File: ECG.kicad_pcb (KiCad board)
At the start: 4 copper layers, 60 x 60 mm, 94 parts, among them J1 SJ-3566AN, J2 Conn_01x02_Male, J3 Conn_01x08_Male, J4 Conn_01x02_Male, J5 Conn_ARM_JTAG_SWD_10, Q1 BC858, U1 ADR4525, U2 LTC3531, U3 INA333, U4 OPA388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

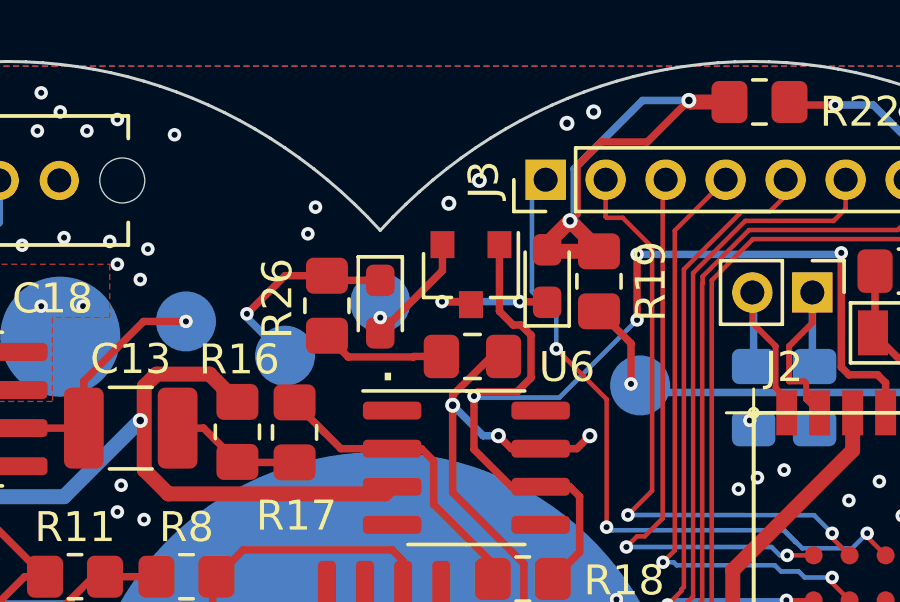
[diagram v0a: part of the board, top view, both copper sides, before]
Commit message: #24 - Update layout with flipped PNP and update images
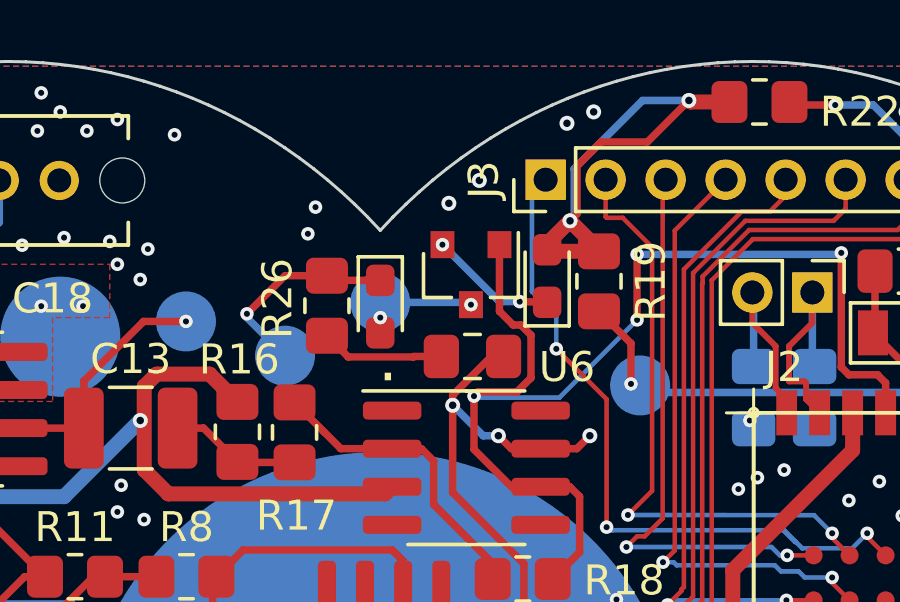
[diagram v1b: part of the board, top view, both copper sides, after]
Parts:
- R14: value 1k -> 10k
- R15: value 100k -> 10k
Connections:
- Q1 pad 2: Net-(D3-Pad2) -> Net-(D1-Pad1)
- Q1 pad 3: Net-(D1-Pad1) -> Net-(D3-Pad2)
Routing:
- net Net-(D3-Pad2): track 3.80 -> 3.20 mm, vias 1 -> 2

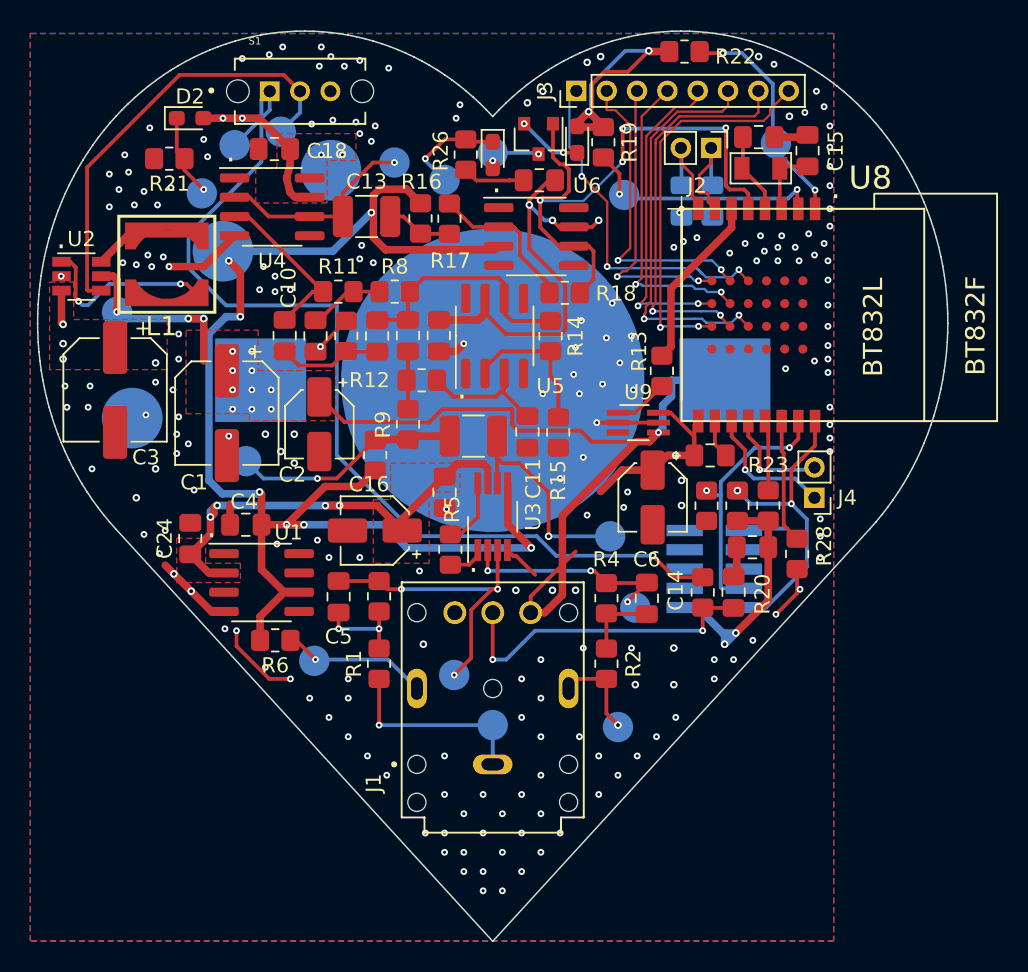
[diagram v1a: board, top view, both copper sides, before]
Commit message: Added mounting holes, Added lead-detect to a micro GPIO, and removed requirement that the leads must be attached prior to turning on the device
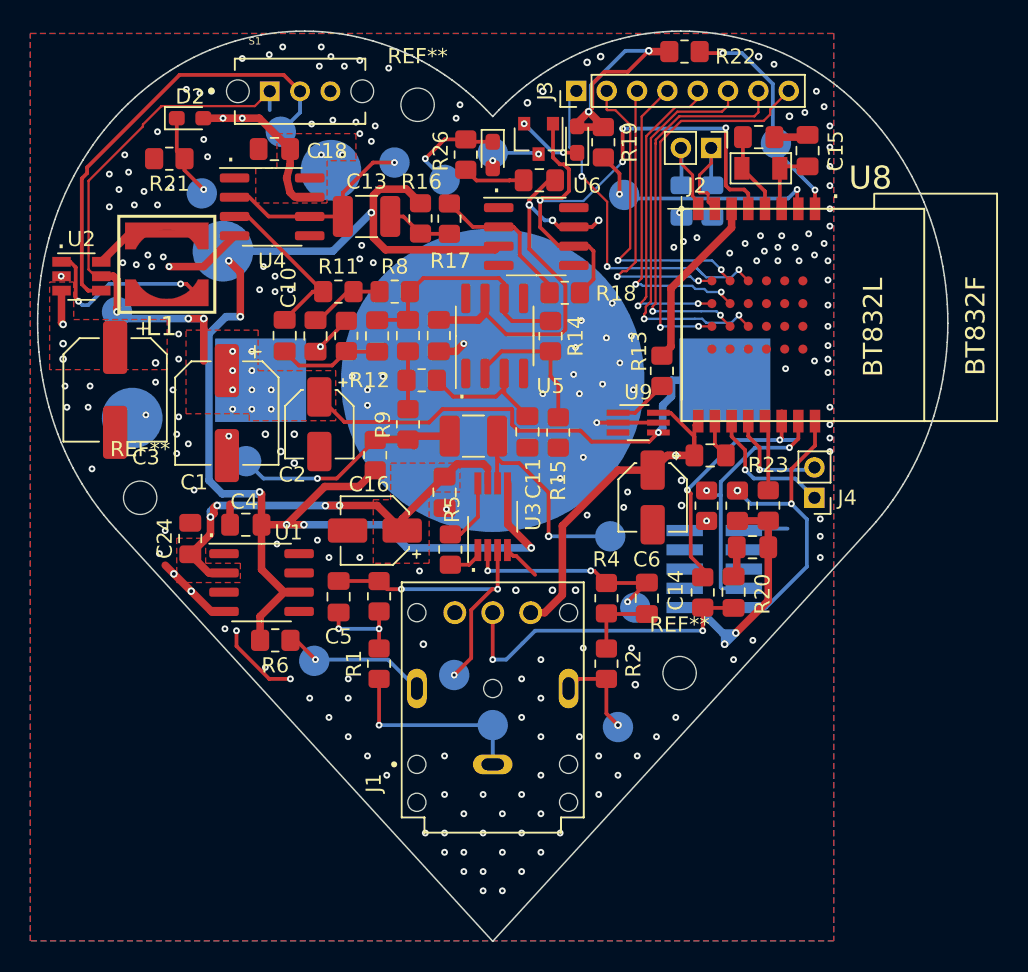
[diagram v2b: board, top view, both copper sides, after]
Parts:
- removed R28: 2k, Resistor_SMD:R_0805_2012Metric_Pad1.20x1.40mm_HandSolder
- removed TP9: TestPoint, TestPoint:TestPoint_Pad_D2.0mm
- added REF**: MountingHole_2.2mm_M2, MountingHole:MountingHole_2.2mm_M2, F.Cu at (128.5, 111.3)
- added REF**: MountingHole_2.2mm_M2, MountingHole:MountingHole_2.2mm_M2, F.Cu at (164.1, 122.8)
- added REF**: MountingHole_2.2mm_M2, MountingHole:MountingHole_2.2mm_M2, F.Cu at (146.8, 85.3)
- C10, C8: value 5n -> 4.7n
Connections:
- J1 pad 6: Vbatt -> 3.3V
- R20 pad 1: Net-(R20-Pad1) -> LEAD_DETECT
- S1 pad 1: Net-(R20-Pad1) -> Vbatt
- U8 pad P$14: Net-(R28-Pad2) -> LEAD_DETECT
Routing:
- net Net-(R20-Pad1): track 66.5 -> 0.00 mm, vias 1 -> 0
- net LEAD_DETECT: track 0.00 -> 17.4 mm, vias 0 -> 2
- net 3.3V: track 130.5 -> 141.1 mm
- net Net-(R28-Pad2): track 8.83 -> 0.00 mm
- net Vbatt: track 65.4 -> 68.0 mm
- net GND: track 52.9 -> 51.1 mm, vias 203 -> 202

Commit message: Updated revision on PCB
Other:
- board text added: "HealthHub 1.0.2"
- board text removed: "HealthHub 1.0.1"

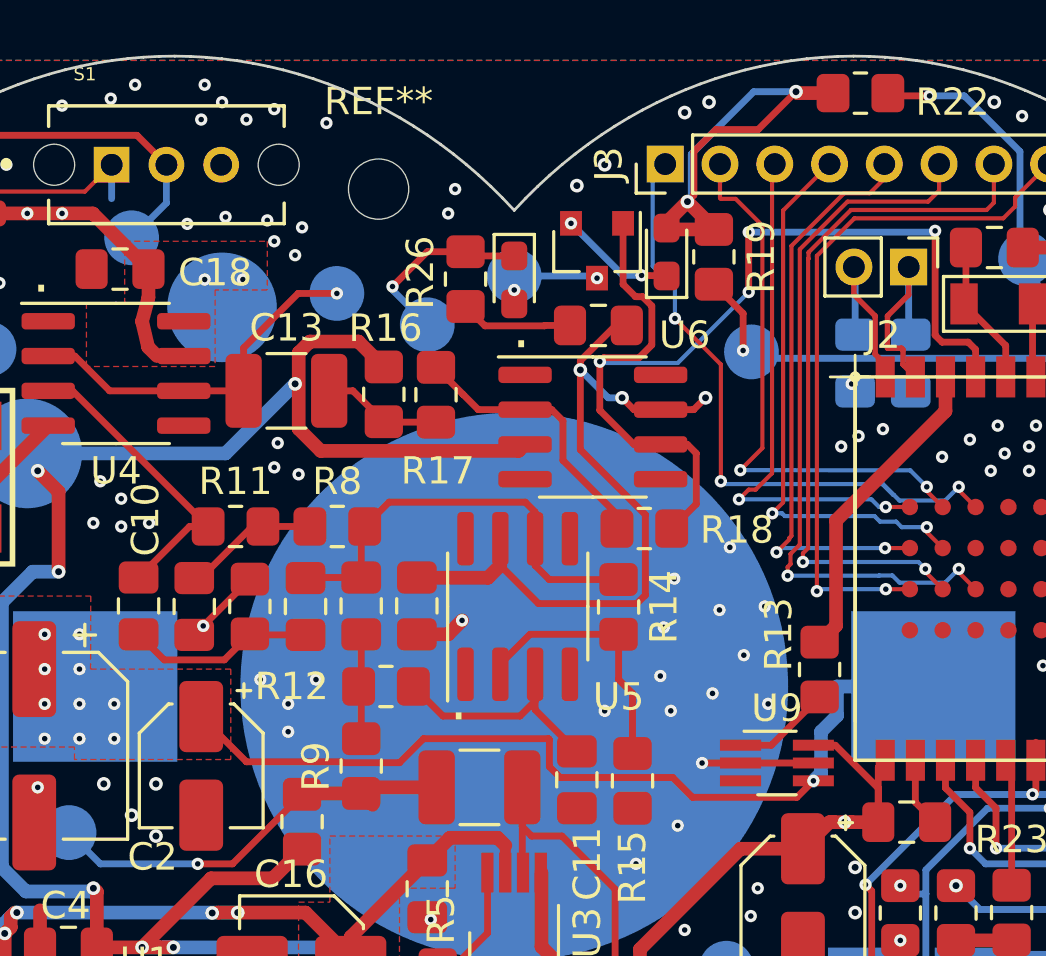
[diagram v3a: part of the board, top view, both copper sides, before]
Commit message: Connected high side power switcher enable pin to SHDN net instead of 3.3V. Prevents feedback on the 3.3V net from registering as a logic high and keeping the power going through
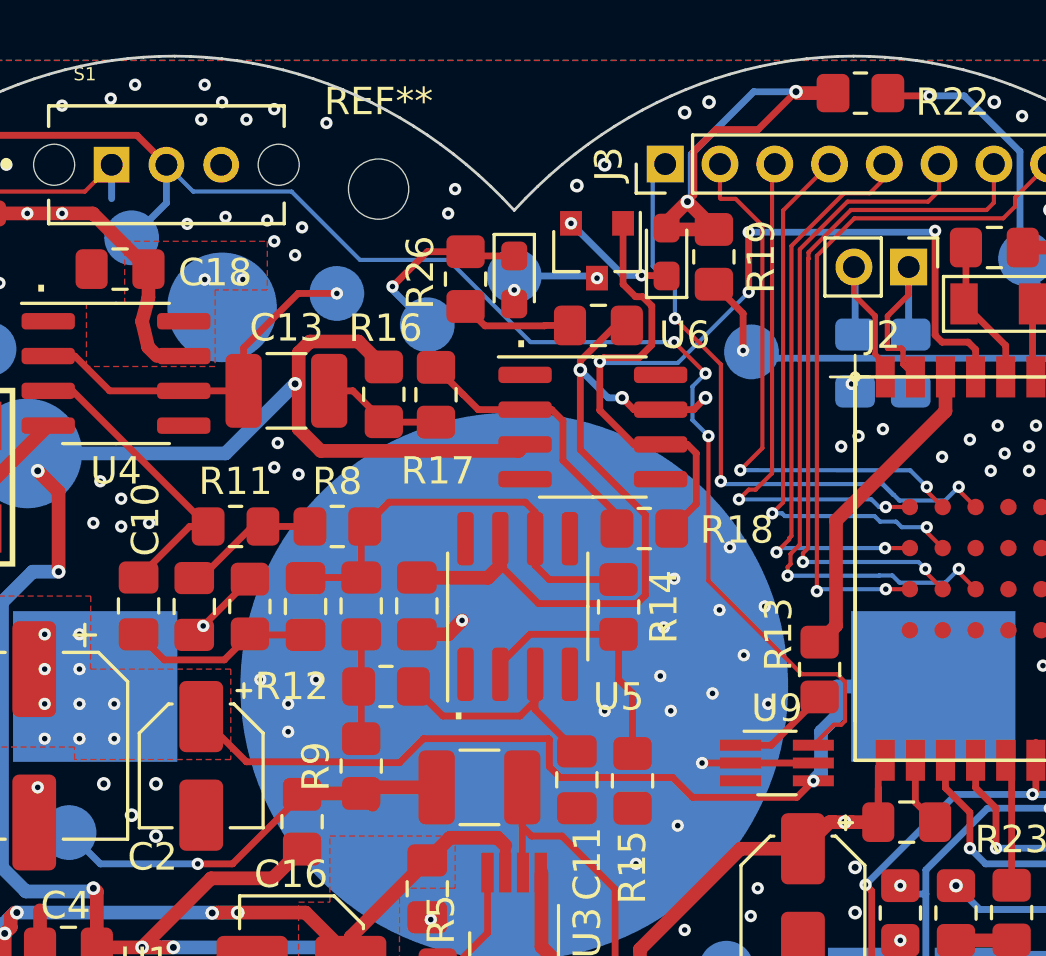
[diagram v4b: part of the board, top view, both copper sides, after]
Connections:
- U9 pad 6: 3.3V -> SHDN
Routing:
- net SHDN: track 29.6 -> 69.9 mm, vias 0 -> 3
- net 3.3V: track 141.1 -> 138.1 mm

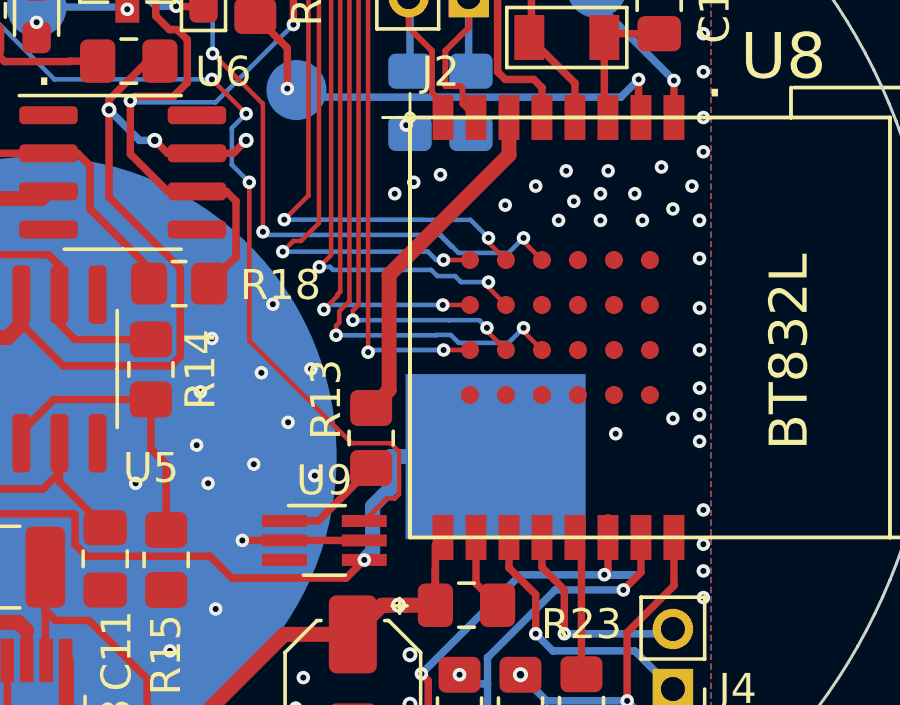
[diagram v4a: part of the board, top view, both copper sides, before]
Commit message: #25 - Updated low pass filter. Gain 2x -> 1x. Added ADC divider for battery to account for brand new batteries.
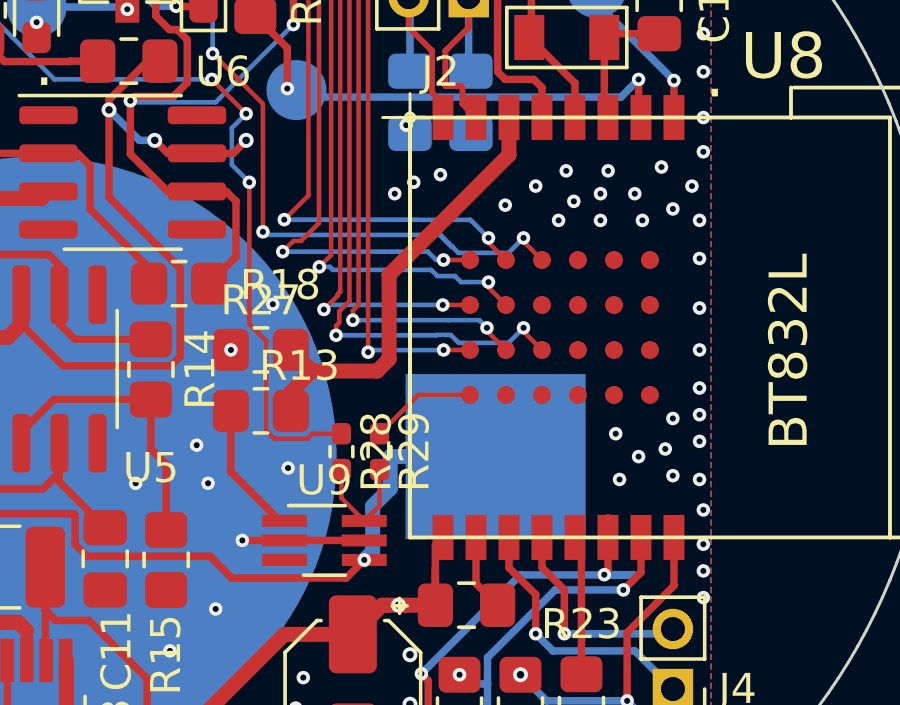
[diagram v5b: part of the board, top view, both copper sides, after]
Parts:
- added R27: 330k, Resistor_SMD:R_0805_2012Metric_Pad1.20x1.40mm_HandSolder, F.Cu at (159.2, 99.9)
- added R28: 0, Resistor_SMD:R_0402_1005Metric_Pad0.72x0.64mm_HandSolder, F.Cu at (161.9, 103.3)
- added R29: 0, Resistor_SMD:R_0402_1005Metric_Pad0.72x0.64mm_HandSolder, F.Cu at (163.2, 103.3)
- R13: value 1k -> 110k
- R15: value 10k -> 100k
- moved R13 3.78 mm to (159.2, 102.0), turned to 180 degrees
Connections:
- U9 pad 6: SHDN -> Net-(R28-Pad2)
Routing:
- net Net-(R28-Pad2): track 0.00 -> 3.95 mm
- net SHDN: track 69.9 -> 66.4 mm
- net Net-(R29-Pad1): track 0.00 -> 3.55 mm
- net Net-(R13-Pad1): track 12.7 -> 16.2 mm
- net Net-(R13-Pad2): track 3.69 -> 4.49 mm

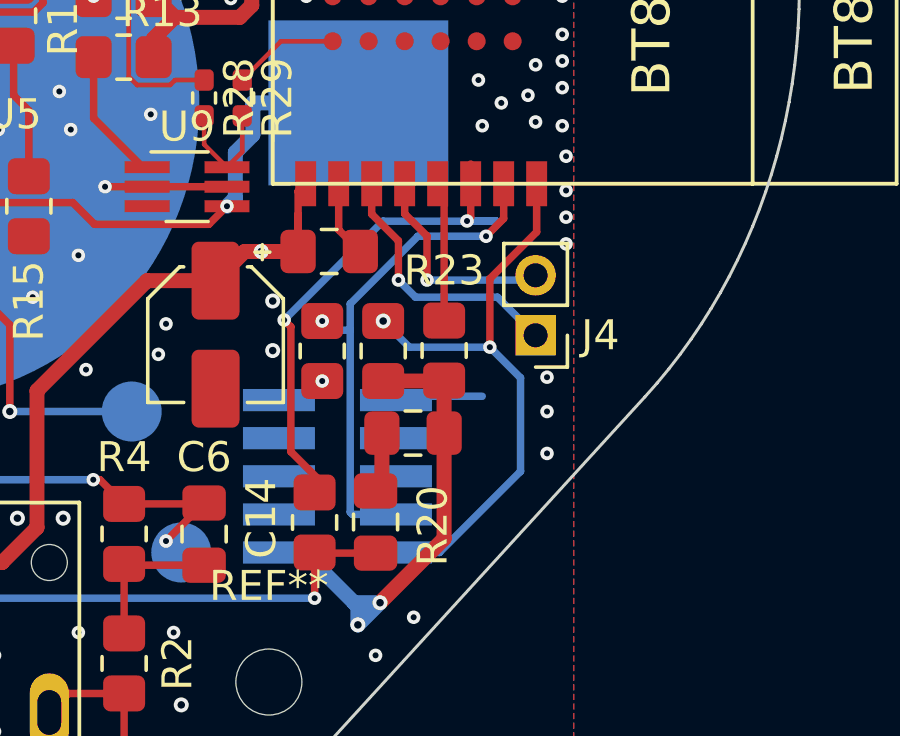
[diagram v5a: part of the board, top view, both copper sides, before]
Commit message: #28 - Remove pulldown from reset line on micro
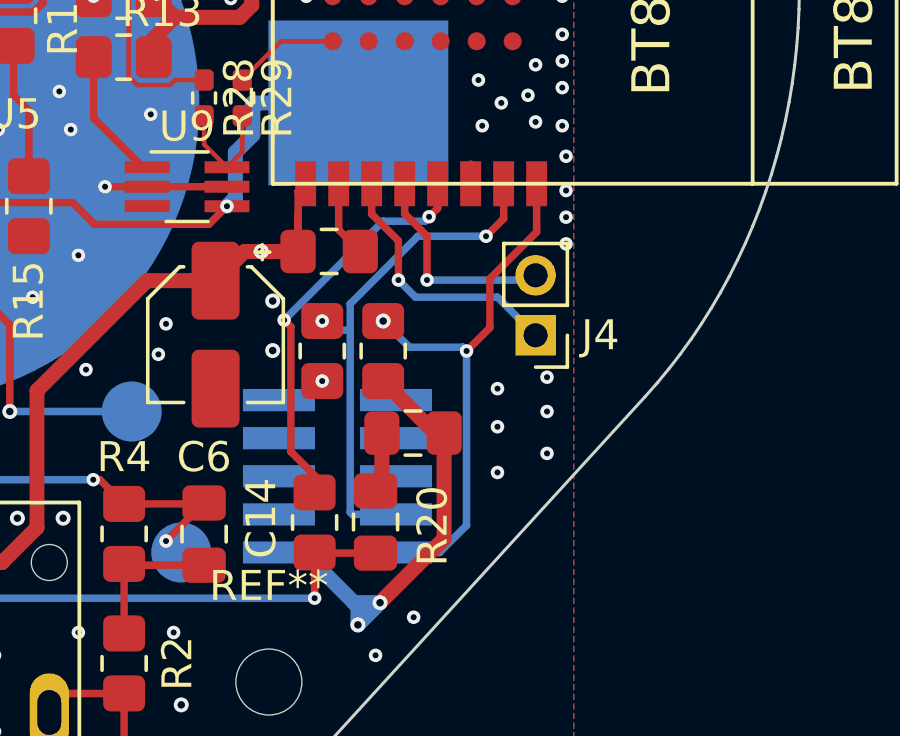
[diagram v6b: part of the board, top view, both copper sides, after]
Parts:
- removed R23: 10k, Resistor_SMD:R_0805_2012Metric_Pad1.20x1.40mm_HandSolder
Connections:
- U8 pad P$13: Net-(R23-Pad1) -> LEAD_DETECT
- U8 pad P$14: LEAD_DETECT -> Net-(U8-PadP$14)
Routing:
- net Net-(R23-Pad1): track 4.65 -> 0.00 mm
- net LEAD_DETECT: track 17.4 -> 13.8 mm
- net Net-(J5-Pad10): track 2.93 -> 0.18 mm
- net Net-(J5-Pad2): track 19.8 -> 18.3 mm
- net 3.3V: track 138.1 -> 137.0 mm
- net Net-(U8-PadP$14): track 0.00 -> 0.66 mm
- net GND: vias 202 -> 205

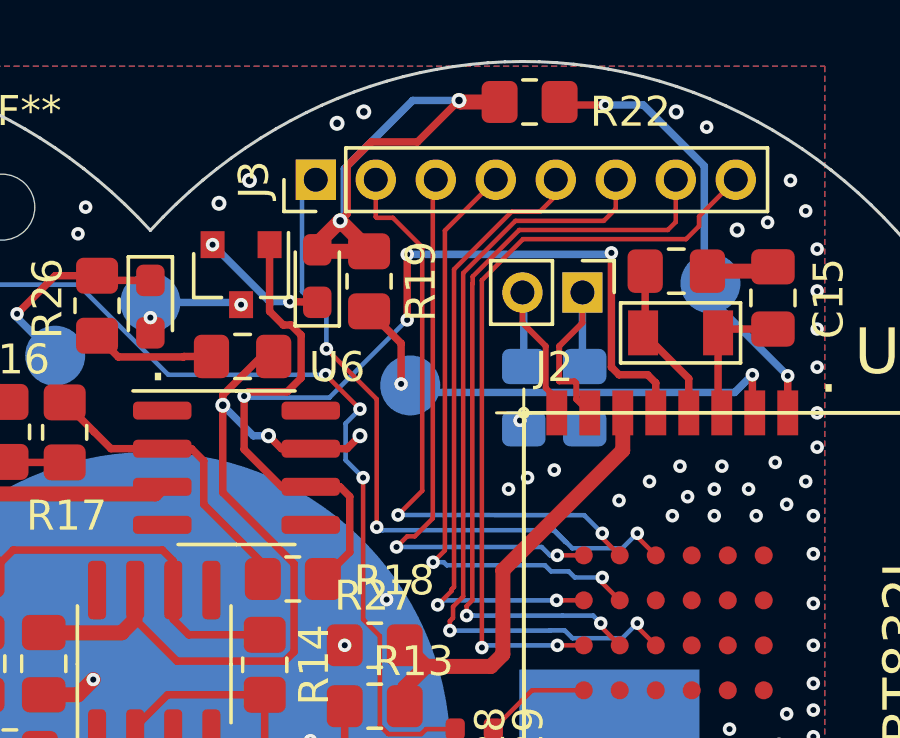
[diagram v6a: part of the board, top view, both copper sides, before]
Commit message: Updated debug header to include 3.3V and GND
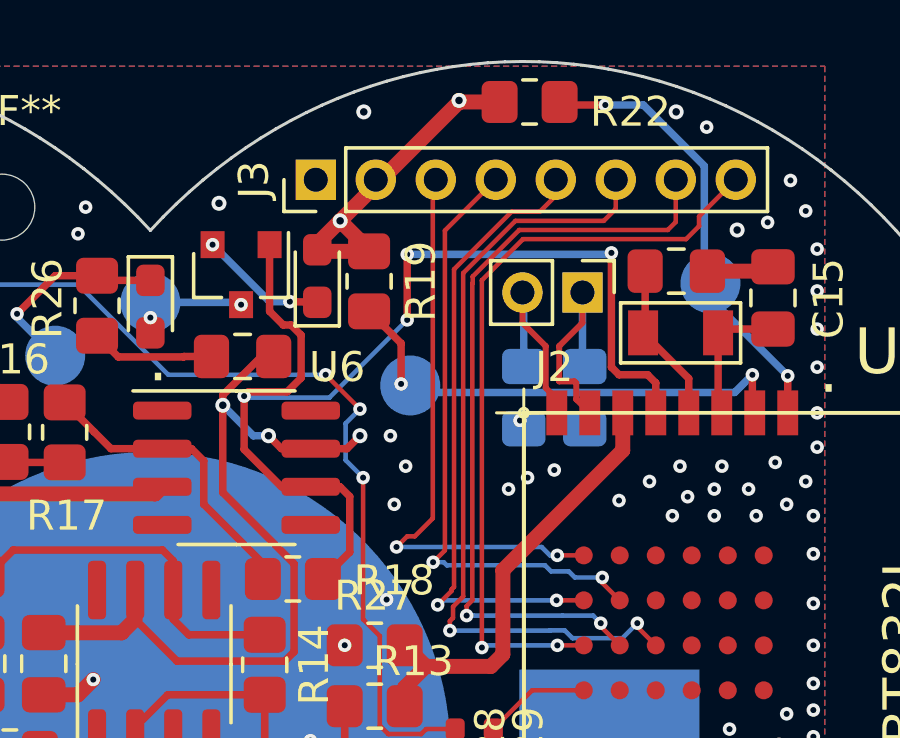
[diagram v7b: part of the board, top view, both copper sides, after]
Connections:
- J3 pad 1: Net-(J3-Pad1) -> GND
- J3 pad 2: Net-(J3-Pad2) -> 3.3V
- U8 pad P$A3: Net-(J3-Pad1) -> Net-(U8-PadP$A3)
- U8 pad P$A4: Net-(J3-Pad2) -> Net-(U8-PadP$A4)
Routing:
- net Net-(J3-Pad1): track 23.6 -> 0.00 mm, vias 3 -> 0
- net Net-(J3-Pad2): track 20.5 -> 0.00 mm, vias 2 -> 0
- net 3.3V: track 137.0 -> 129.6 mm, vias 24 -> 22
- net GND: track 51.1 -> 51.7 mm, vias 205 -> 208
